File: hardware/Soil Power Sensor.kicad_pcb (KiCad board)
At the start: 2 copper layers, 139 x 45 mm, 75 parts, among them J1 Screw_Terminal_01x05, J2 RFShield_OnePiece, J3 UART, J4 Conn_01x03, J5 Micro_SD_Card, J7 Conn_01x04_Socket, Q1 BSS123, SW1 BOOT, SW2 EN, SW3 SW_DP3T, U1 MAX9944, U10 Wio-E5 mini, U11 MB85RC1MT, U12 MB85RC1MT, U2 INA296A, U3 REF2033, U4 THS4532, U5 TPS60400DBV, U6 ADS1219, U7 SN74LVC1G240, U8 ESP32-C3-WROOM-02-N4

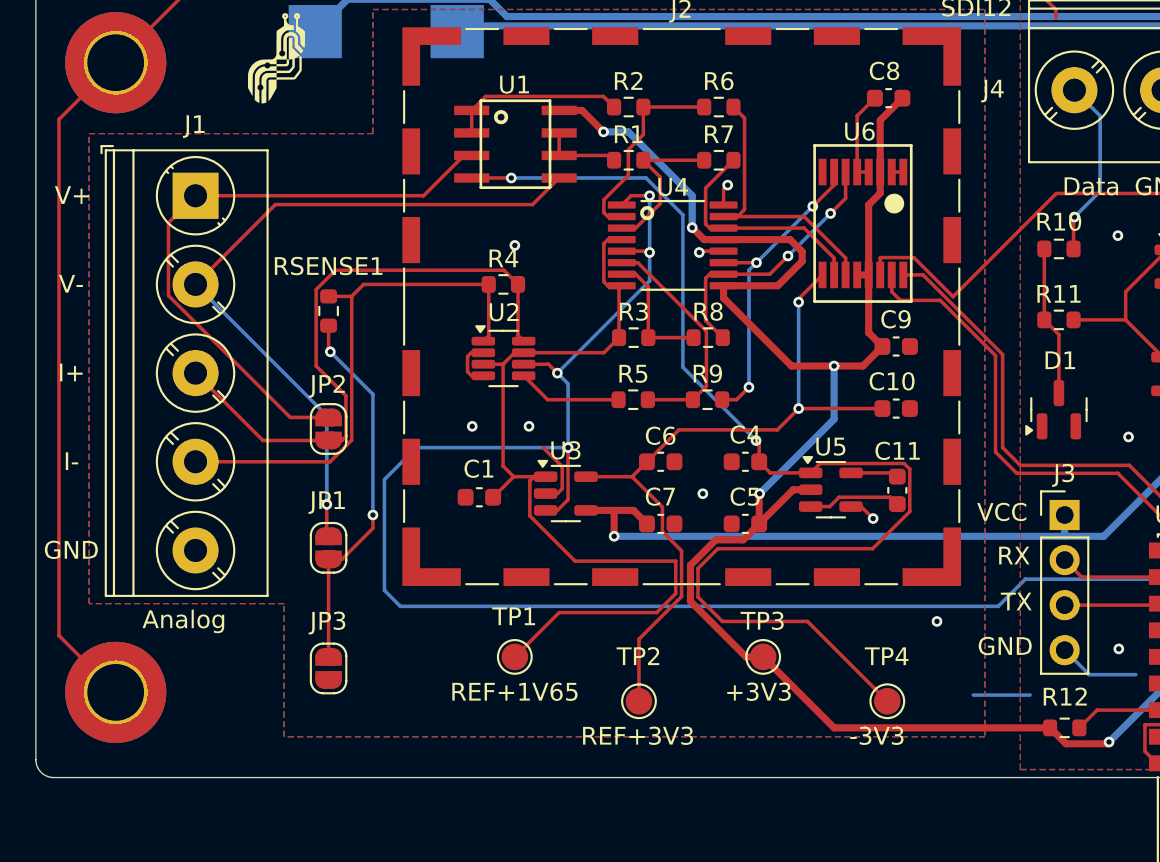
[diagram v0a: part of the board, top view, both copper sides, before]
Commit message: Moved silkscreen for analog terminals
Closes #51
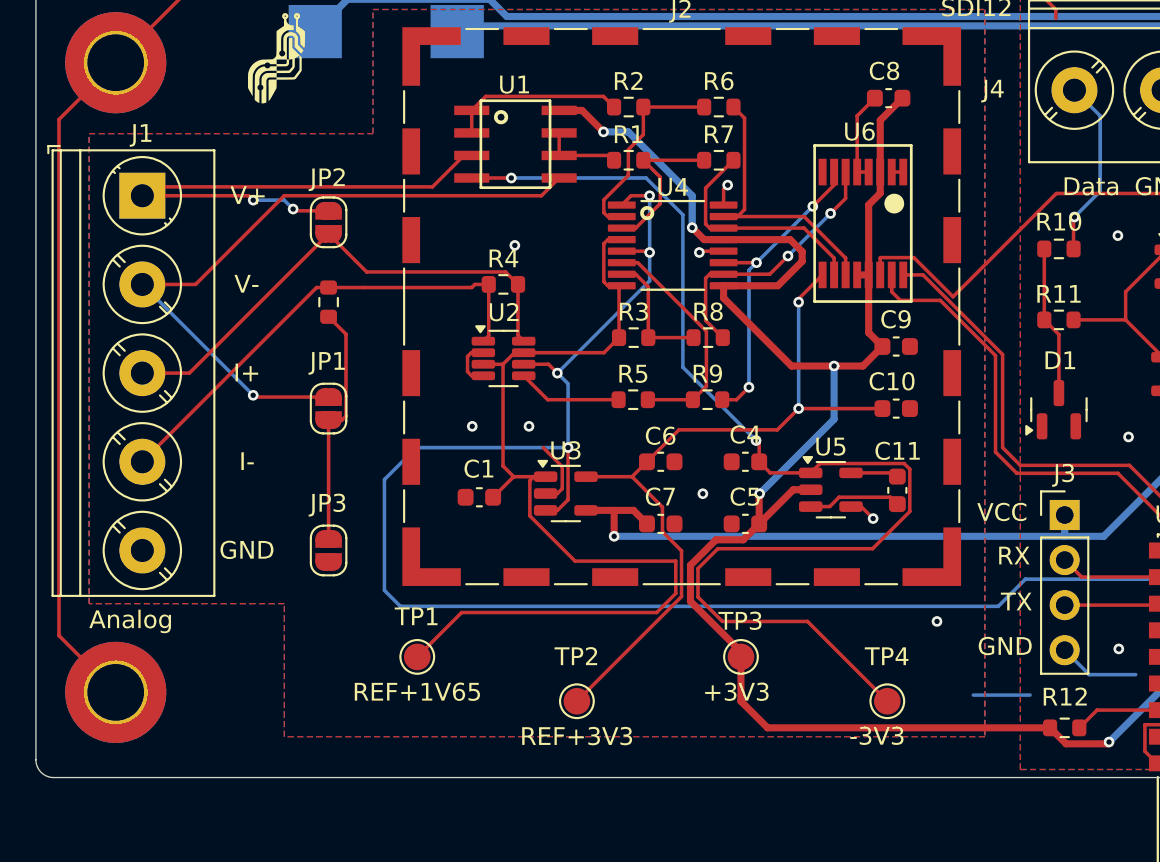
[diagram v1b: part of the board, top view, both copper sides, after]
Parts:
- moved JP2 11.7 mm to (128.5, 60.5)
- moved JP1 7.85 mm to (128.5, 71.0)
- moved JP3 6.65 mm to (128.5, 79.0)
- moved TP1 5.50 mm to (133.5, 85.0)
- moved TP2 3.50 mm to (142.5, 87.5)
- moved J1 3.00 mm to (118.0, 59.0)
- moved TP3 1.25 mm to (151.8, 85.0)
- moved RSENSE1 0.50 mm to (128.5, 65.0)
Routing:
- net Net-(JP1-A): track 21.2 -> 13.8 mm, vias 2 -> 0
- net /Analog/I+: track 34.6 -> 28.9 mm
- net REF+1V65: track 50.3 -> 55.8 mm
- net /Analog/V+: track 34.6 -> 30.4 mm, vias 0 -> 2
- net /Analog/I-: track 30.1 -> 27.0 mm
- net +3V3: track 290.6 -> 292.2 mm
- net REF+3V3: track 41.2 -> 42.7 mm
- net /Analog/V-: track 40.3 -> 39.1 mm

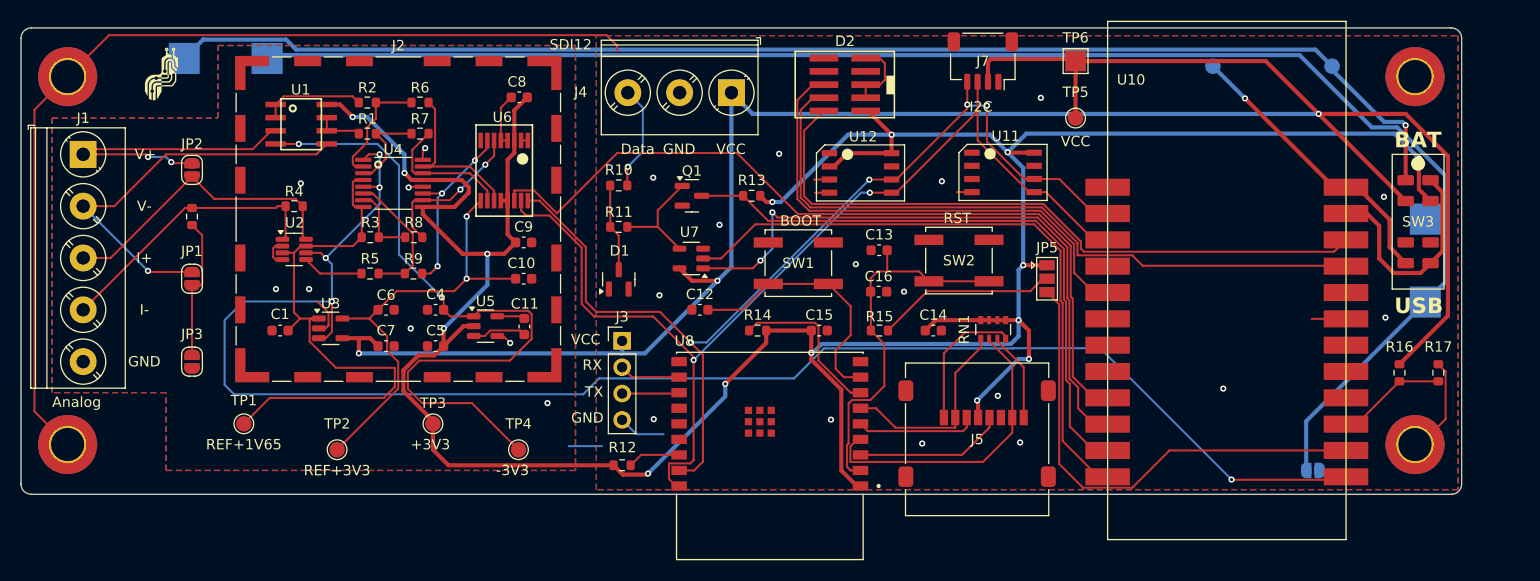
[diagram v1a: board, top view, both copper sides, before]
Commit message: Fixed microSD card
Closes #54
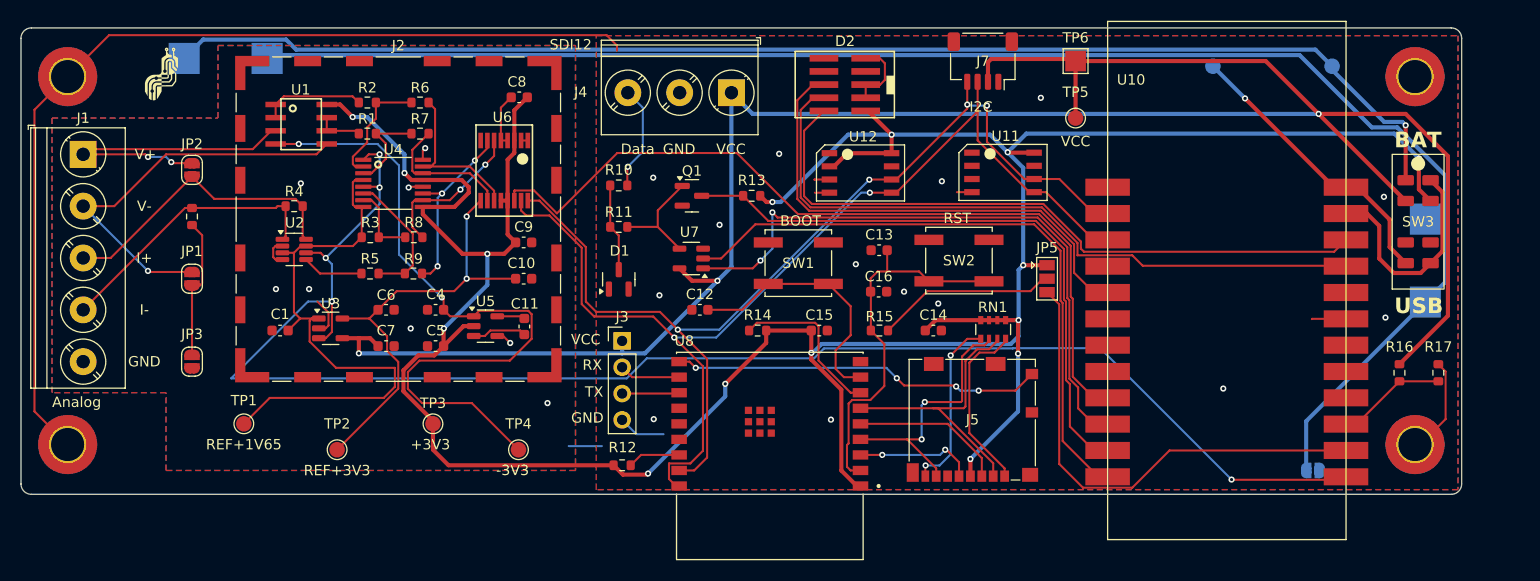
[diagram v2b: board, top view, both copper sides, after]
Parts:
- J5: footprint Connector_Card:microSD_HC_Molex_47219-2001 -> Connector_Card:microSD_HC_Molex_104031-0811
- moved J5 1.95 mm to (203.8, 84.6), turned to 180 degrees
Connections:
- RN1 pad 1: /ESP32/CS -> Net-(J5-DAT1)
- RN1 pad 3: Net-(J5-DAT1) -> /ESP32/CS
- U8 pad 10: unconnected-(U8-IO10-Pad10) -> /ESP32/CD
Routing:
- net /ESP32/CD: track 0.00 -> 35.9 mm, vias 0 -> 4
- net Net-(J5-DAT1): track 8.65 -> 17.0 mm, vias 0 -> 2
- net /ESP32/CS: track 19.5 -> 27.7 mm
- net /Analog/POWERDOWN: track 159.7 -> 153.5 mm
- net +3V3: track 292.2 -> 297.2 mm
- net /ESP32/SDO: track 29.5 -> 25.7 mm, vias 0 -> 2
- net Net-(J5-DAT2): track 13.4 -> 17.0 mm
- net /ESP32/SDI: track 11.6 -> 14.8 mm
- net /ESP32/CLK: track 14.5 -> 11.6 mm, vias 0 -> 2
- net /STM32/SDA: track 101.4 -> 103.1 mm
- net /STM32/SCL: track 97.6 -> 98.7 mm
- net GND: vias 24 -> 22

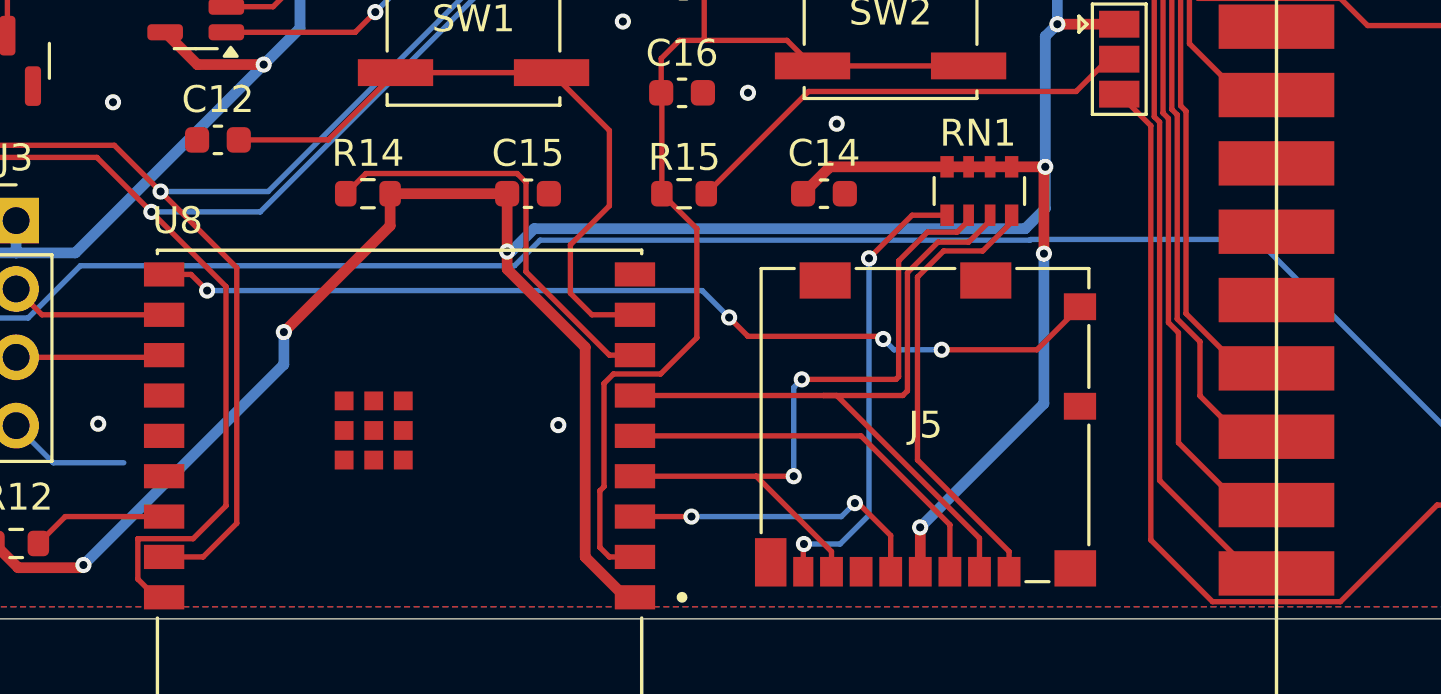
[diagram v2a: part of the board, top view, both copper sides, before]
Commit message: Added wakeup line for esp32
Closes #48
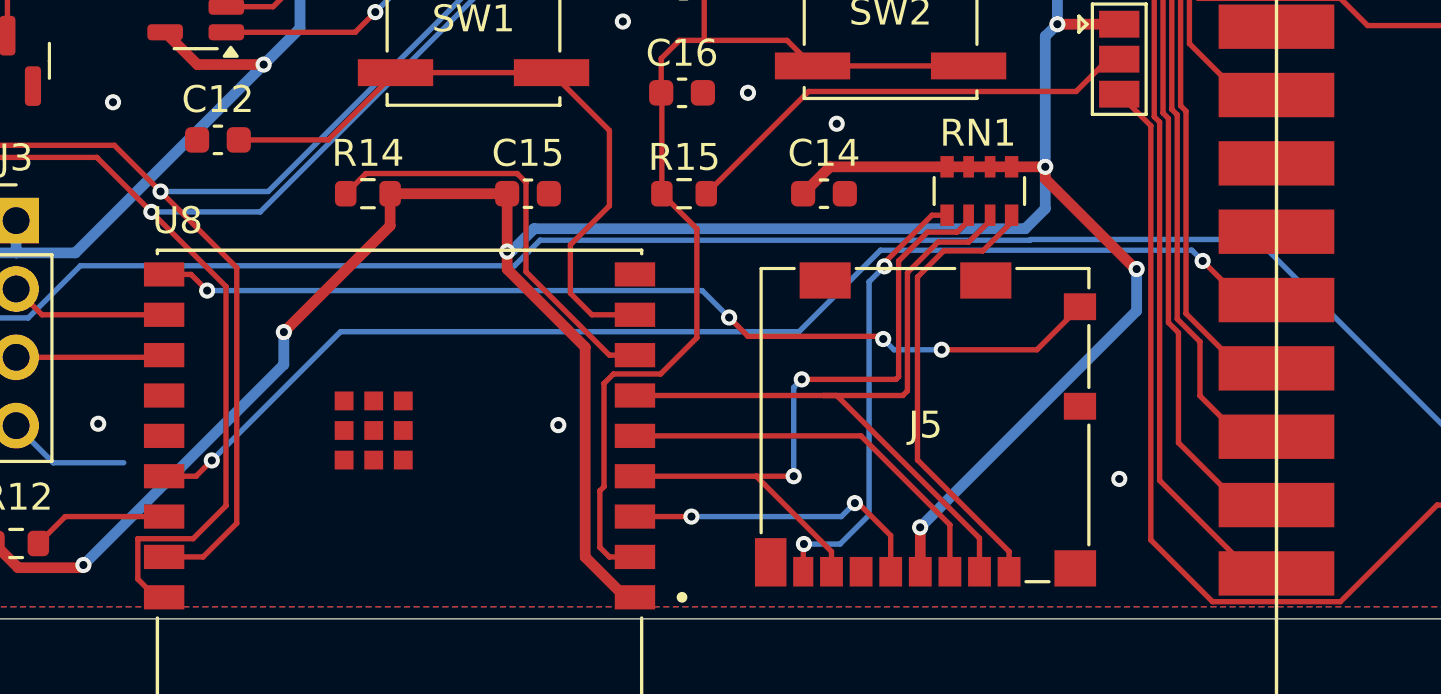
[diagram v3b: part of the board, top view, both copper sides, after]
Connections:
- U10 pad 8: unconnected-(U10-PA0/D0-Pad8) -> /ESP32/WAKEUP
- U8 pad 15: unconnected-(U8-IO3-Pad15) -> /ESP32/WAKEUP
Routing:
- net /ESP32/WAKEUP: track 0.00 -> 45.6 mm, vias 0 -> 2
- net +3V3: track 297.2 -> 300.0 mm
- net GND: vias 22 -> 23

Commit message: Fixed misc issues during ordering
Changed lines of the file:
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@@
 		(tags "microSD SD molex")
 		(property "Reference" "J5"
-			(at 0 0 360)
+			(at 0 0 0)
 			(layer "F.SilkS")
 			(effects
@@
 		)
 		(property "Value" "Micro_SD_Card"
-			(at 0 7.39 360)
+			(at 0 7.39 0)
 			(layer "F.Fab")
 			(effects
@@
 		)
 		(fp_text user "${REFERENCE}"
-			(at 0 0 360)
+			(at 0 0 0)
 			(layer "F.Fab")
 			(effects
@@
 		)
 		(fp_circle
-			(center 9.6 -1.2)
-			(end 10.232456 -1.2)
-			(stroke
-				(width 0.1)
+			(center -1.4 -1.2)
+			(end -0.767544 -1.2)
+			(stroke
+				(width 0.1)

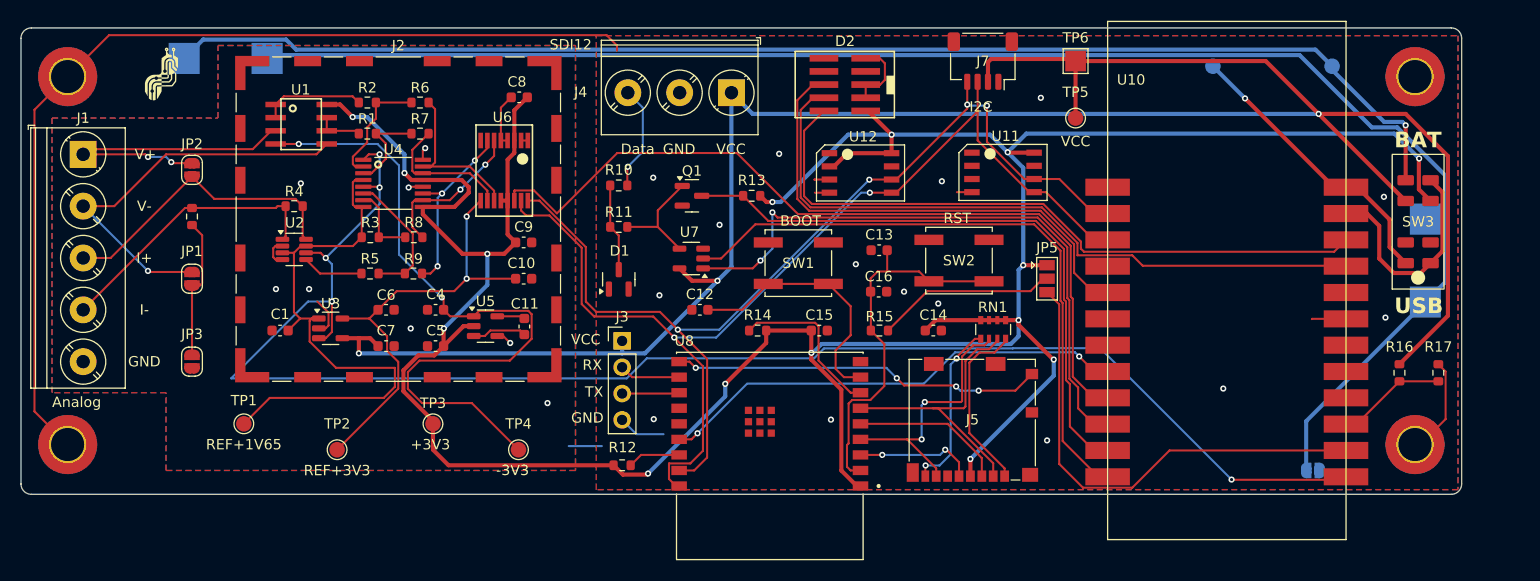
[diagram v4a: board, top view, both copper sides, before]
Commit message: Removed power switch
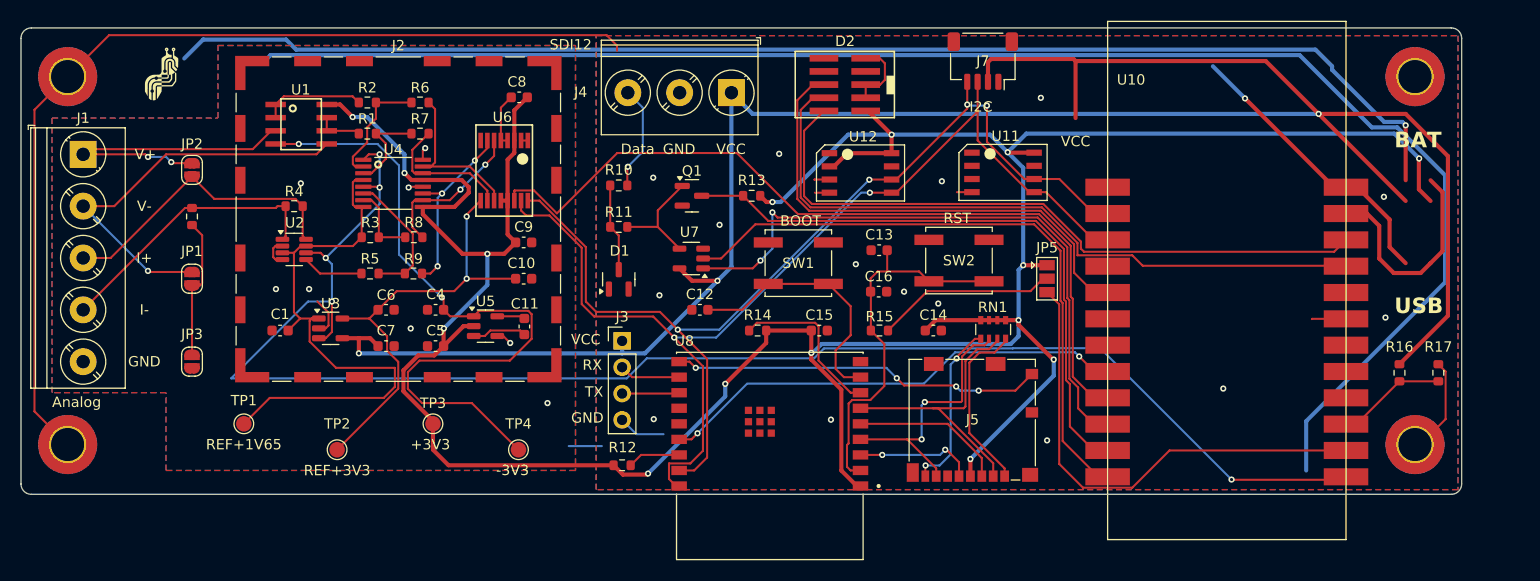
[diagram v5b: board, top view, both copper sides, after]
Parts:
- removed G1: BAT1, Soil Power Sensor:Keystone2463
- removed G2: BAT2, Soil Power Sensor:Keystone2463
- removed JP4: SolderJumper_2_Open, Jumper:SolderJumper-2_P1.3mm_Open_RoundedPad1.0x1.5mm
- removed SW3: SW_DP3T, Soil Power Sensor:JS203011JCQN
- removed TP5: VCC, TestPoint:TestPoint_Pad_D1.5mm
- removed TP6: +, TestPoint:TestPoint_Pad_2.0x2.0mm
- removed TP7: VUSB, TestPoint:TestPoint_Pad_D1.5mm
- removed TP8: VBAT, TestPoint:TestPoint_Pad_D1.5mm
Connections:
- U10 pad 23: /STM32/STM_3V3 -> +3V3
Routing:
- net (no net): track 0.00 -> 280.2 mm, vias 0 -> 1
- net /Power/VBAT_SPLIT: track 152.6 -> 0.00 mm
- net /Power/VBAT: track 127.5 -> 0.00 mm, vias 1 -> 0
- net /STM32/STM_3V3: track 21.7 -> 0.00 mm
- net +3V3: track 300.0 -> 321.8 mm
